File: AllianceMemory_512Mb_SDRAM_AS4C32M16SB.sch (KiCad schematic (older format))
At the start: 1 part

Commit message: batch push
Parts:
- gave numbers to parts that had none: 1
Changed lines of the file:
@@
 P 5350 1350
 AR Path="/5F5DA166/5F9046D8" Ref="SDRAM?"  Part="1"
-AR Path="/5F5DA166/5F902D84/5F9046D8" Ref="SDRAM?"  Part="1"
-AR Path="/5F5DA166/5FA0E635/5F9046D8" Ref="SDRAM?"  Part="1"
-F 0 "SDRAM?" H 5700 1515 50  0000 C CNN
+AR Path="/5F5DA166/5F902D84/5F9046D8" Ref="SDRAM1"  Part="1"
+AR Path="/5F5DA166/5FA0E635/5F9046D8" Ref="SDRAM2"  Part="1"
+F 0 "SDRAM1" H 5700 1515 50  0000 C CNN
 F 1 "AllianceMemory_512M_SDRAM_Bdie_AS4C32M16SB" H 5700 1424 50  0000 C CNN
 F 2 "" H 5350 1350 50  0001 C CNN
@@
 	5250 1650 4600 1650
 $Comp
-L power:+3V3 #PWR?
+L power:+3V3 #PWR021
 U 1 1 5F905239
 P 4600 1250
-AR Path="/5F5DA166/5F902D84/5F905239" Ref="#PWR?"  Part="1"
-AR Path="/5F5DA166/5FA0E635/5F905239" Ref="#PWR?"  Part="1"
-F 0 "#PWR?" H 4600 1100 50  0001 C CNN
+AR Path="/5F5DA166/5F902D84/5F905239" Ref="#PWR021"  Part="1"
+AR Path="/5F5DA166/5FA0E635/5F905239" Ref="#PWR025"  Part="1"
+F 0 "#PWR025" H 4600 1100 50  0001 C CNN
 F 1 "+3V3" H 4615 1423 50  0000 C CNN
 F 2 "" H 4600 1250 50  0001 C CNN
@@
 	6150 1950 6950 1950
 $Comp
-L power:+3V3 #PWR?
+L power:+3V3 #PWR023
 U 1 1 5F916182
 P 6950 1250
-AR Path="/5F5DA166/5F902D84/5F916182" Ref="#PWR?"  Part="1"
-AR Path="/5F5DA166/5FA0E635/5F916182" Ref="#PWR?"  Part="1"
-F 0 "#PWR?" H 6950 1100 50  0001 C CNN
+AR Path="/5F5DA166/5F902D84/5F916182" Ref="#PWR023"  Part="1"
+AR Path="/5F5DA166/5FA0E635/5F916182" Ref="#PWR027"  Part="1"
+F 0 "#PWR027" H 6950 1100 50  0001 C CNN
 F 1 "+3V3" H 6965 1423 50  0000 C CNN
 F 2 "" H 6950 1250 50  0001 C CNN
@@
 $EndComp
 $Comp
-L power:GND #PWR?
+L power:GND #PWR022
 U 1 1 5F91B1FC
 P 6750 1250
-AR Path="/5F5DA166/5F902D84/5F91B1FC" Ref="#PWR?"  Part="1"
-AR Path="/5F5DA166/5FA0E635/5F91B1FC" Ref="#PWR?"  Part="1"
-F 0 "#PWR?" H 6750 1000 50  0001 C CNN
+AR Path="/5F5DA166/5F902D84/5F91B1FC" Ref="#PWR022"  Part="1"
+AR Path="/5F5DA166/5FA0E635/5F91B1FC" Ref="#PWR026"  Part="1"
+F 0 "#PWR026" H 6750 1000 50  0001 C CNN
 F 1 "GND" H 6755 1077 50  0000 C CNN
 F 2 "" H 6750 1250 50  0001 C CNN
@@
 	4350 2550 5250 2550
 $Comp
-L power:GND #PWR?
+L power:GND #PWR020
 U 1 1 5F91CB3E
 P 4350 1250
-AR Path="/5F5DA166/5F902D84/5F91CB3E" Ref="#PWR?"  Part="1"
-AR Path="/5F5DA166/5FA0E635/5F91CB3E" Ref="#PWR?"  Part="1"
-F 0 "#PWR?" H 4350 1000 50  0001 C CNN
+AR Path="/5F5DA166/5F902D84/5F91CB3E" Ref="#PWR020"  Part="1"
+AR Path="/5F5DA166/5FA0E635/5F91CB3E" Ref="#PWR024"  Part="1"
+F 0 "#PWR024" H 4350 1000 50  0001 C CNN
 F 1 "GND" H 4355 1077 50  0000 C CNN
 F 2 "" H 4350 1250 50  0001 C CNN

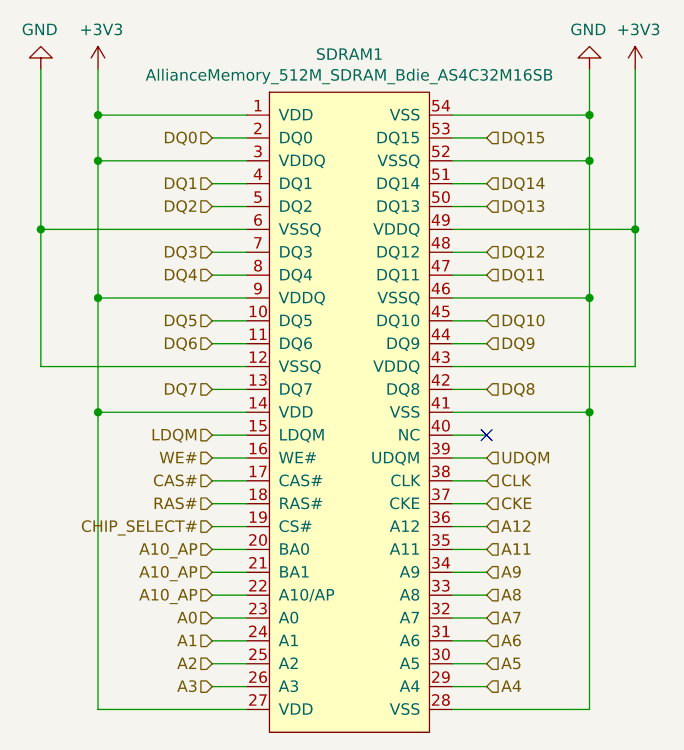
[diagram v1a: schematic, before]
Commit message: Added XTALs, Removed WIP Initialization and Added NPXLPCOPEN
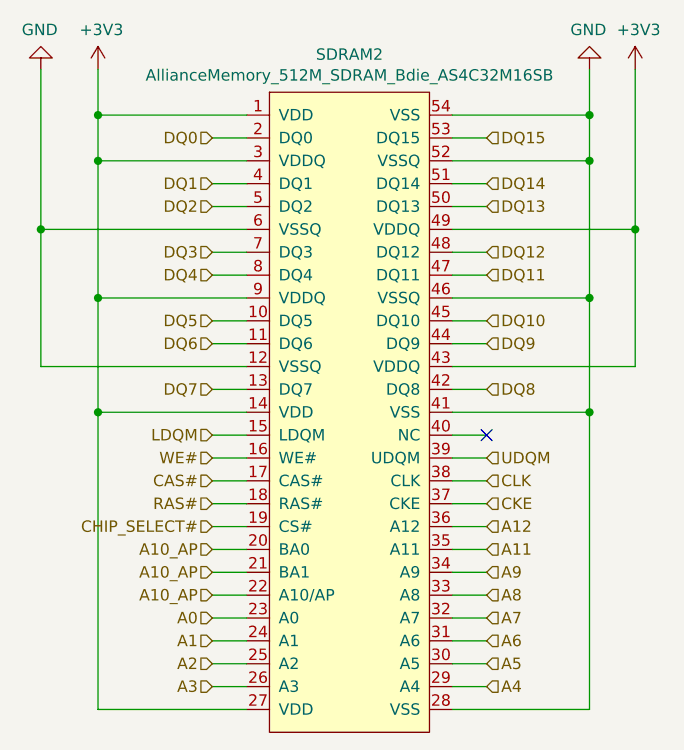
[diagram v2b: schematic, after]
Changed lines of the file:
@@
 $Descr A4 11693 8268
 encoding utf-8
-Sheet 6 7
+Sheet 7 7
 Title ""
 Date ""
@@
 AR Path="/5F5DA166/5F902D84/5F9046D8" Ref="SDRAM1"  Part="1"
 AR Path="/5F5DA166/5FA0E635/5F9046D8" Ref="SDRAM2"  Part="1"
-F 0 "SDRAM1" H 5700 1515 50  0000 C CNN
+F 0 "SDRAM2" H 5700 1515 50  0000 C CNN
 F 1 "AllianceMemory_512M_SDRAM_Bdie_AS4C32M16SB" H 5700 1424 50  0000 C CNN
 F 2 "" H 5350 1350 50  0001 C CNN
